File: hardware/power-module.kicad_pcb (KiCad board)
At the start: 4 copper layers, 85 x 50 mm, 80 parts, among them CN1 WJ2EDGRC-5.08-2P, J1 Conn_01x04_Pin, K1 SRA-12VDC-CL, K2 SRA-12VDC-CL, K3 SRA-12VDC-CL, K4 SRA-12VDC-CL, P1 WJ2EDGRC-5.08-4P, Q1 SS8050_C2150, Q2 SS8050_C2150, U1 AMS1117-3.3_C347222, U10 XL-1010RGBC-WS2812B, U11 XL-1010RGBC-WS2812B, U12 XL-1010RGBC-WS2812B, U13 L327S400H11L, U14 UMW78L05, U15 XL-1010RGBC-WS2812B, U16 XL-1010RGBC-WS2812B, U17 XL-1010RGBC-WS2812B, U18 XL-1010RGBC-WS2812B, U2 CC6903SO-10A, U3 W5500, U4 ESP32-C3FH4, U5 AMS1117-3.3_C347222, U6 XL-1010RGBC-WS2812B, U7 DP9900LP-12V, U8 XL-1010RGBC-WS2812B, U9 XL-1010RGBC-WS2812B, X1 X49SM25MSD2SC

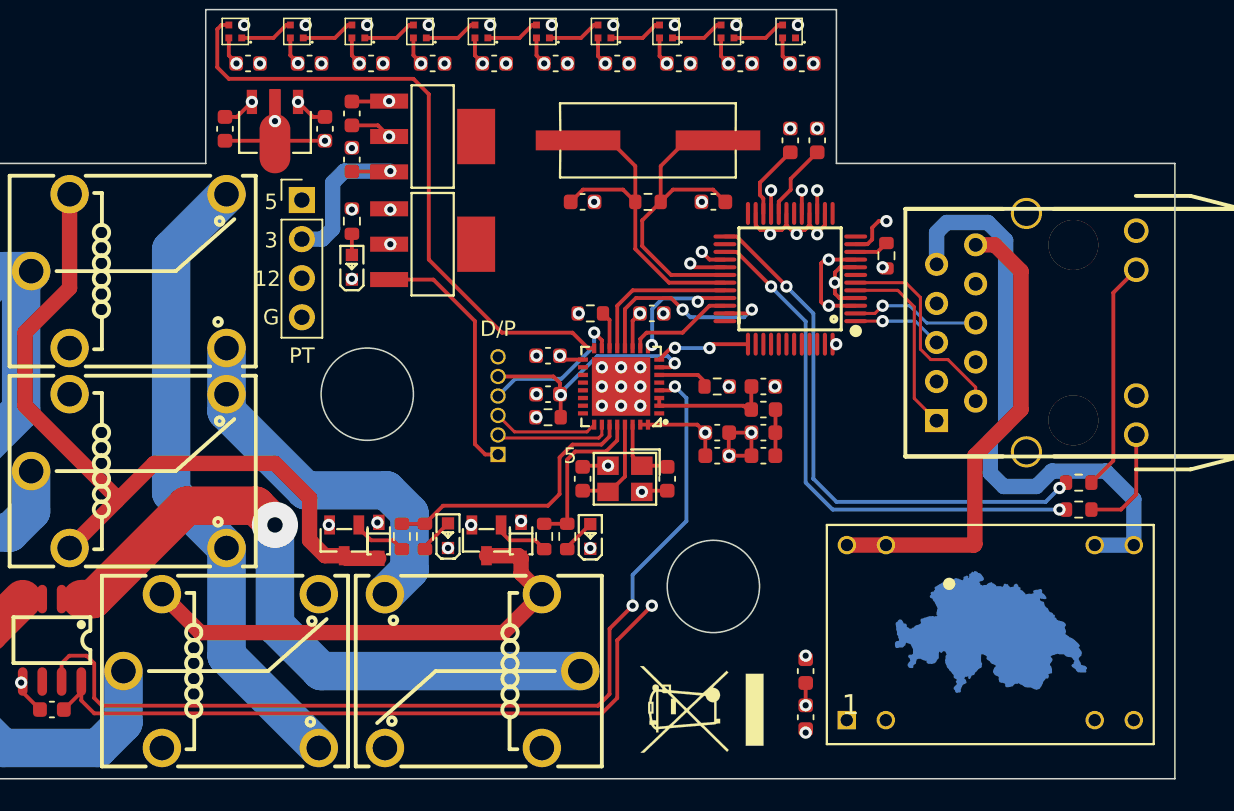
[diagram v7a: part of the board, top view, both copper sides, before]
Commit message: Fix crystal
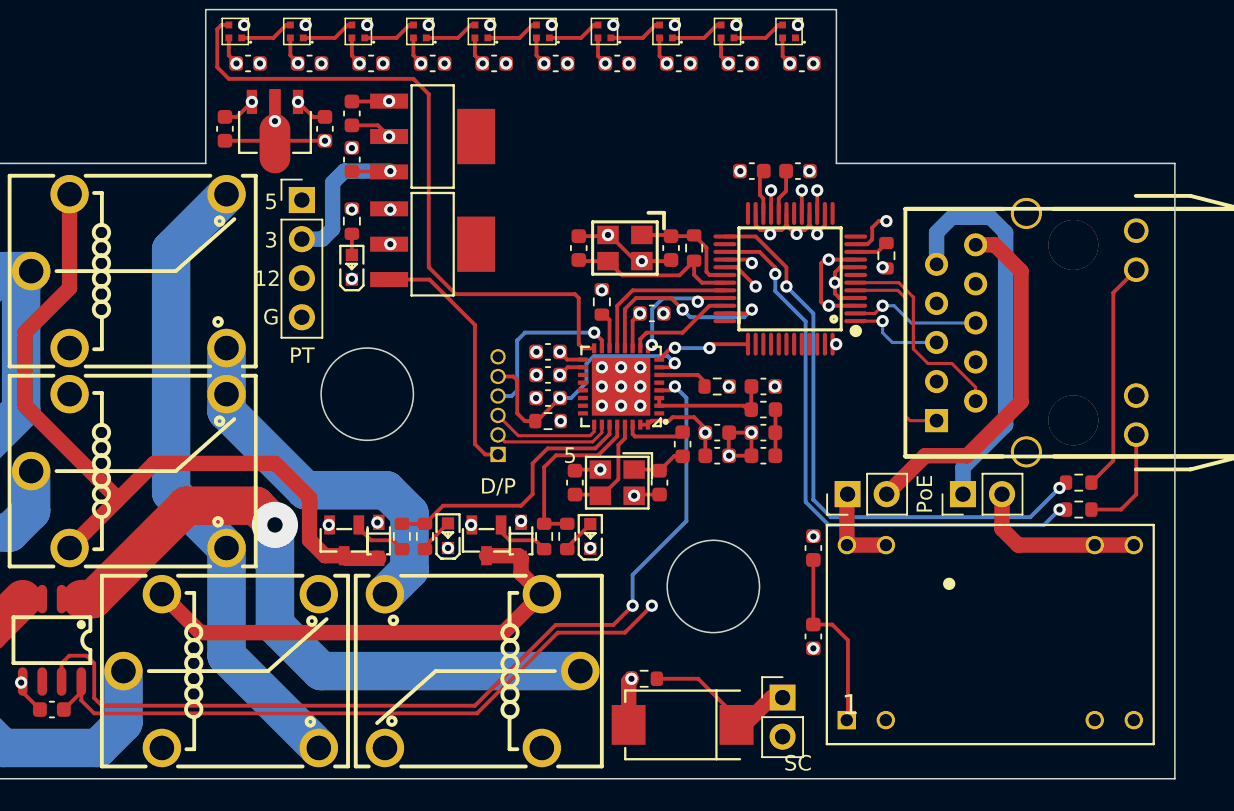
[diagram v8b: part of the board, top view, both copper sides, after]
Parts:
- removed REF**: WEEE-Logo_5.6x8mm_SilkScreen, Symbol:WEEE-Logo_5.6x8mm_SilkScreen
- added C32: TAJE337M016RNJ, easyeda2kicad:CAP-SMD_L7.3-W4.3-R-RD, F.Cu at (53.0, 46.5)
- added C33: 1uF, Capacitor_SMD:C_0603_1608Metric, F.Cu at (44.2, 23.8)
- added J2: Conn_01x02, Connector_PinHeader_2.54mm:PinHeader_1x02_P2.54mm_Vertical, F.Cu at (63.7, 31.5)
- added J3: Conn_01x02, Connector_PinHeader_2.54mm:PinHeader_1x02_P2.54mm_Vertical, F.Cu at (71.2, 31.5)
- added J4: Conn_01x02, Connector_PinHeader_2.54mm:PinHeader_1x02_P2.54mm_Vertical, F.Cu at (59.5, 44.7)
- added L2: 24nH, Inductor_SMD:L_0603_1608Metric, F.Cu at (53.0, 28.2)
- added R13: 6.2k, Resistor_SMD:R_0603_1608Metric, F.Cu at (50.5, 43.5)
- C16, C17: value 1uF -> 14pF
- C7, C8: value 4.7uF -> 18pF
- X1: value X49SM25MSD2SC -> X322525MRB4SI; footprint easyeda2kicad:HC-49S_L11.4-W4.8 -> easyeda2kicad:OSC-SMD_4P-L3.2-W2.5-BL_SIT8008BI
- moved C3 8.02 mm to (61.5, 35.0)
- moved X1 7.16 mm to (49.2, 15.5), turned to 180 degrees
- moved C4 5.27 mm to (61.5, 40.8)
- moved R6 4.24 mm to (53.8, 15.5), turned to 90 degrees
- moved C7 4.07 mm to (52.2, 15.5), turned to -90 degrees
- moved C6 3.20 mm to (57.5, 10.5), turned to 180 degrees
- moved C8 3.01 mm to (46.2, 15.5), turned to 90 degrees
- moved C5 2.36 mm to (60.5, 10.5), turned to 0 degrees
- moved R12 1.06 mm to (47.8, 19.0), turned to -90 degrees
- moved C16 0.56 mm to (51.5, 30.8)
- moved C17 0.56 mm to (46.0, 30.8)
- moved U13 0.56 mm to (48.8, 30.8)
- moved C24 0.25 mm to (44.2, 22.2)
- moved C9 0.25 mm to (44.2, 25.2)
- moved R9 0.25 mm to (44.2, 26.8), turned to 0 degrees
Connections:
- C16 pad 2: Net-(U4-XTAL_P) -> Net-(C16-Pad2)
- RJ1 pad 10: /POE IN - -> Net-(J2-Pin_2)
- RJ1 pad 9: /POE IN + -> Net-(J3-Pin_1)
- U13 pad 1: Net-(U4-XTAL_P) -> Net-(C16-Pad2)
- U4 pad 18: unconnected-(U4-VDD_SPI-Pad18) -> +3.3V
- X1 pad 1: Net-(U3-XO) -> Net-(U3-XI/CLKIN)
- X1 pad 2: Net-(U3-XI/CLKIN) -> GND
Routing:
- net /POE IN +: track 39.2 -> 11.3 mm
- net Net-(J3-Pin_1): track 0.00 -> 25.5 mm
- net /POE IN -: track 31.0 -> 5.87 mm
- net Net-(J2-Pin_2): track 0.00 -> 23.4 mm
- net Net-(U3-XI/CLKIN): track 21.8 -> 7.44 mm
- net +12V: track 15.6 -> 26.3 mm, vias 5 -> 4
- net GND: track 55.1 -> 65.2 mm, vias 63 -> 65
- net Net-(J4-Pin_1): track 0.00 -> 10.2 mm
- net Net-(U3-XO): track 21.5 -> 11.4 mm
- net Net-(C16-Pad2): track 0.00 -> 3.56 mm
- net /CURRENT SENSING INPUT: track 63.5 -> 61.0 mm
- net /LED ACTIVITY: track 35.3 -> 37.7 mm
- net /LED LINK: track 36.1 -> 38.5 mm
- net Net-(U3-TOCAP): track 5.01 -> 2.95 mm
- net /LED DATA IN: track 41.7 -> 43.8 mm
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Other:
- board text added: "PoE"
- board text added: "SC"
